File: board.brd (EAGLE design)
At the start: 80 x 80 mm, 47 parts, among them U1 MAX232

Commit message: added gitignore, tweaked board
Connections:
- removed net N$2: U1.12
- removed net N$20: U1.9
- removed net N$21: U1.10
- removed net N$9: U1.11
- net PC2: now also U1.12
- net PC3: now also U1.11
- net PC6: now also U1.9
- net PC7: now also U1.10
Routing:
- net PC2: track 25.1 -> 40.2 mm
- net PC7: track 12.8 -> 26.1 mm
- net PC3: track 23.2 -> 35.6 mm
- net PC6: track 16.4 -> 26.3 mm
- net GND: vias 21 -> 24
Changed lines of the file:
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@@
 <via x="69" y="63" extent="1-16" drill="0.305" shape="octagon"/>
 <contactref element="C3" pad="-"/>
+<via x="23" y="77" extent="1-16" drill="0.305" shape="octagon"/>
+<via x="24" y="73" extent="1-16" drill="0.305" shape="octagon"/>
+<via x="22" y="71" extent="1-16" drill="0.305" shape="octagon"/>
 <wire x1="44.784" y1="69.094" x2="44.784" y2="65.118" width="0" layer="19" extent="1-1"/>
 </signal>
@@
 <wire x1="33.608" y1="73.754" x2="29.417" y2="77.945" width="0.254" layer="1"/>
 <wire x1="29.417" y1="77.945" x2="27.385" y2="77.945" width="0.254" layer="1"/>
+<contactref element="U1" pad="12"/>
+<wire x1="15.635" y1="72.6" x2="15.635" y2="74.635" width="0.254" layer="1"/>
+<wire x1="15.635" y1="74.635" x2="18.945" y2="77.945" width="0.254" layer="1"/>
+<wire x1="18.945" y1="77.945" x2="27.385" y2="77.945" width="0.254" layer="1"/>
 </signal>
 <signal name="PC3">
@@
 <wire x1="32.592" y1="72.738" x2="32.592" y2="63.928478125" width="0.254" layer="1"/>
 <wire x1="32.592" y1="63.928478125" x2="38.281875" y2="58.238603125" width="0.254" layer="1"/>
+<contactref element="U1" pad="11"/>
+<wire x1="16.905" y1="72.6" x2="17" y2="72.695" width="0.4064" layer="1"/>
+<wire x1="17" y1="72.695" x2="17" y2="74" width="0.254" layer="1"/>
+<wire x1="17" y1="74" x2="18.405" y2="75.405" width="0.254" layer="1"/>
+<wire x1="18.405" y1="75.405" x2="27.385" y2="75.405" width="0.254" layer="1"/>
 </signal>
 <signal name="PC4">
@@
 <wire x1="29.798" y1="67.658" x2="29.798" y2="63.328365625" width="0.254" layer="1"/>
 <wire x1="29.798" y1="63.328365625" x2="36.58481875" y2="56.541546875" width="0.254" layer="1"/>
+<contactref element="U1" pad="9"/>
+<wire x1="27.385" y1="67.785" x2="22.57" y2="72.6" width="0.254" layer="1"/>
+<wire x1="22.57" y1="72.6" x2="19.445" y2="72.6" width="0.254" layer="1"/>
 </signal>
 <signal name="PC7">
@@
 <wire x1="36.019134375" y1="55.9758625" x2="27.385" y2="64.609996875" width="0.254" layer="1"/>
 <wire x1="27.385" y1="65.245" x2="27.385" y2="64.609996875" width="0.254" layer="1"/>
+<contactref element="U1" pad="10"/>
+<wire x1="22.63" y1="70" x2="27.385" y2="65.245" width="0.254" layer="1"/>
+<wire x1="18.175" y1="72.6" x2="18.175" y2="70.825" width="0.4064" layer="1"/>
+<wire x1="18.175" y1="70.825" x2="19" y2="70" width="0.254" layer="1"/>
+<wire x1="19" y1="70" x2="22.63" y2="70" width="0.254" layer="1"/>
 </signal>
 <signal name="PB0">
@@
 <wire x1="34.712" y1="41.904" x2="34.712" y2="40.226" width="0.254" layer="1"/>
 </signal>
-<signal name="N$2">
-<contactref element="U1" pad="12"/>
-</signal>
-<signal name="N$9">
-<contactref element="U1" pad="11"/>
-</signal>
-<signal name="N$20">
-<contactref element="U1" pad="9"/>
-</signal>
-<signal name="N$21">
-<contactref element="U1" pad="10"/>
-</signal>
 <signal name="AUX-TX">

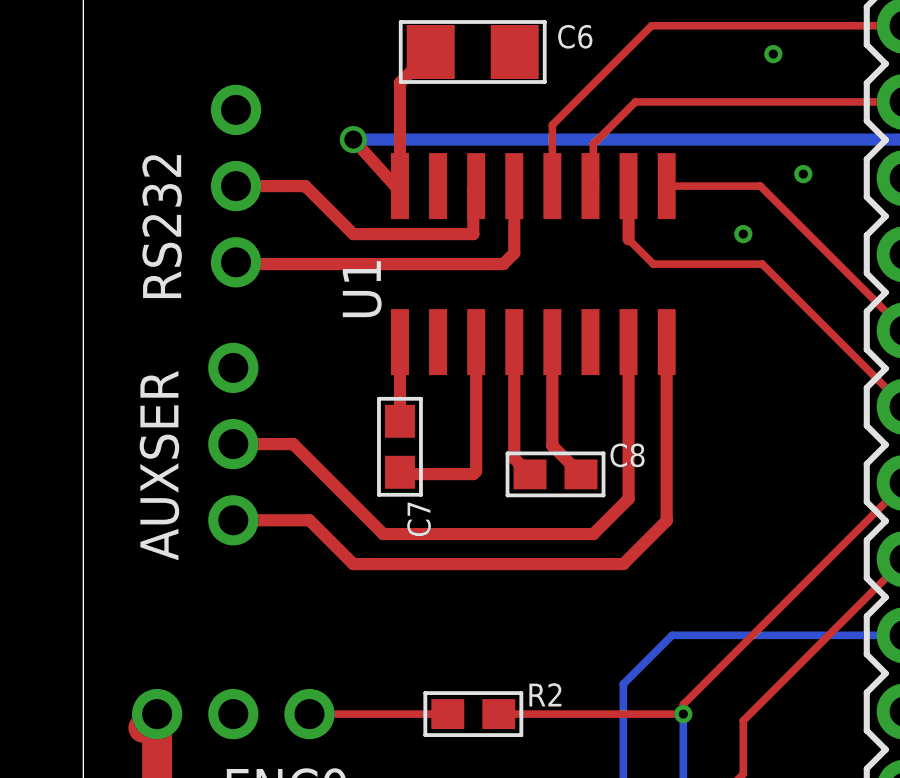
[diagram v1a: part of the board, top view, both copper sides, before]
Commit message: add some part values, nudge some traces
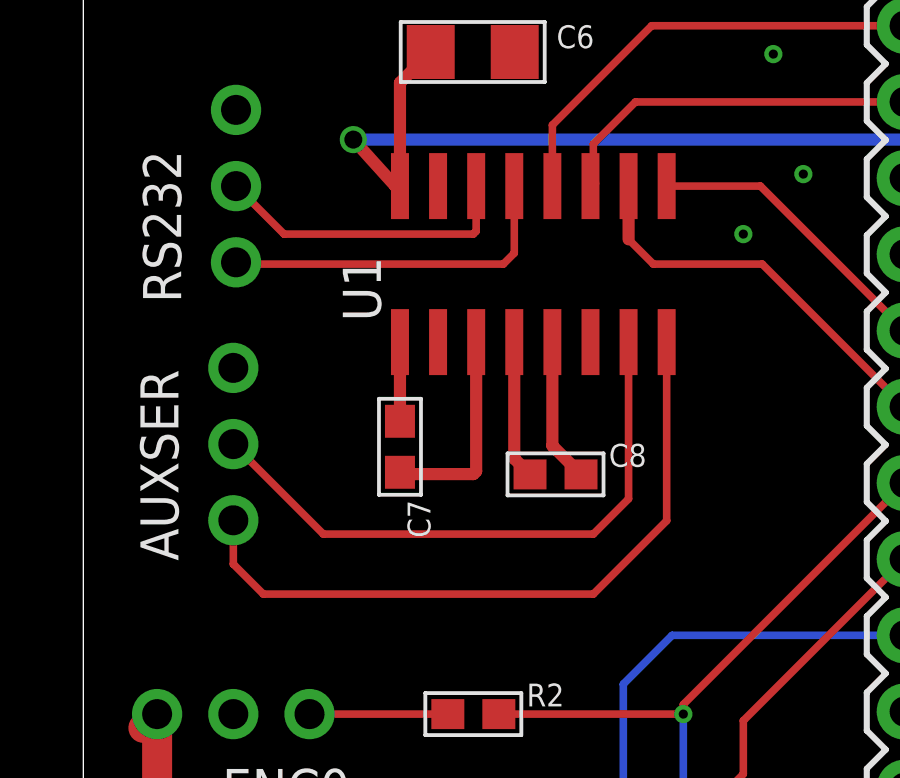
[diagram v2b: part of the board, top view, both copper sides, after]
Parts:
- C10, C9: value (none) -> 0.1uF
- C11: value (none) -> 18pF
- C12: value (none) -> 10pF
- C13, C14: value (none) -> 1uF
- C3: value (none) -> 470uF
- R1: value (none) -> 130O
- R2, R3, R4: value (none) -> 6.8k
- RN1: value (none) -> 10k
- RN2, RN3: value (none) -> 10K
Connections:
- net AUX-RX: now also AUXSER.2, U1.7; no longer AUXSER.1, U1.8
- net AUX-TX: now also AUXSER.1, U1.8; no longer AUXSER.2, U1.7
- net REMUS-RX: now also RS232.2, U1.14; no longer RS232.1, U1.13
- net REMUS-TX: now also RS232.1, U1.13; no longer RS232.2, U1.14
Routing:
- net AUX-TX: track 20.1 -> 23.3 mm
- net REMUS-RX: track 11.7 -> 10.2 mm
- net REMUS-TX: track 10.2 -> 11.7 mm
- net AUX-RX: track 21.6 -> 20.1 mm
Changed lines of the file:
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@@
 <element name="U$1" library="nonolith" package="SO-08" value="PCA9306" x="68.59" y="64.78" rot="R270"/>
 <element name="U1" library="nonolith" package="SO-16" value="MAX232" x="15" y="70"/>
-<element name="RN1" library="nonolith" package="RN8P-4R-CRA06S" value="" x="69.13" y="70.52" rot="R180"/>
+<element name="RN1" library="nonolith" package="RN8P-4R-CRA06S" value="10k" x="69.13" y="70.52" rot="R180"/>
 <element name="U$2" library="nonolith" package="NXT-FOOTPRINT" value="NXT-CONNECTOR" x="72.08" y="54.02" rot="R270"/>
 <element name="PT78" library="nonolith" package="1X03_ROUND" value="" x="11.09" y="16.49" rot="R90"/>
@@
 <element name="C1" library="microbuilder" package="EIA7343-31/D-W" value="470uF" x="62.1" y="75.82" rot="R180"/>
 <element name="C2" library="microbuilder" package="EIA7343-31/D-W" value="470uF" x="63.68" y="36.26"/>
-<element name="C3" library="microbuilder" package="EIA7343-31/D-W" value="" x="20.26" y="23.02" rot="R270"/>
+<element name="C3" library="microbuilder" package="EIA7343-31/D-W" value="470uF" x="20.26" y="23.02" rot="R270"/>
 <element name="C4" library="nonolith" package="1206" value="10uF" x="16.22" y="14.07"/>
 <element name="C5" library="nonolith" package="1206" value="10uF" x="65.4" y="40.93" rot="R180"/>
@@
 <element name="U$6" library="SparkFun" package="1X19" value="M19" x="52.785" y="32.225" smashed="yes" rot="R90"/>
 <element name="U$7" library="SparkFun" package="1X19" value="M19" x="27.385" y="32.225" smashed="yes" rot="R90"/>
-<element name="C9" library="nonolith" package="0603" value="" x="33.989" y="44.544" smashed="yes" rot="R180">
+<element name="C9" library="nonolith" package="0603" value="0.1uF" x="33.989" y="44.544" smashed="yes" rot="R180">
 <attribute name="NAME" x="32.846" y="45.687" size="0.762" layer="25" font="vector" ratio="12"/>
 <attribute name="VALUE" x="32.211" y="45.179" size="0.4064" layer="27" font="vector" rot="R180"/>
 </element>
-<element name="C10" library="nonolith" package="0603" value="" x="40.085" y="64.864" smashed="yes" rot="R180">
+<element name="C10" library="nonolith" package="0603" value="0.1uF" x="40.085" y="64.864" smashed="yes" rot="R180">
 <attribute name="NAME" x="41.609" y="63.594" size="0.762" layer="25" font="vector" ratio="12" rot="R180"/>
 </element>
@@
 <attribute name="VALUE" x="43.514" y="35.448" size="0.8128" layer="25" font="vector" ratio="10" rot="R180"/>
 </element>
-<element name="C11" library="nonolith" package="0603" value="" x="45.038" y="44.036" smashed="yes">
+<element name="C11" library="nonolith" package="0603" value="18pF" x="45.038" y="44.036" smashed="yes">
 <attribute name="NAME" x="43.514" y="42.004" size="0.762" layer="25" font="vector" ratio="12"/>
 </element>
-<element name="C12" library="nonolith" package="0603" value="" x="46.816" y="42.004" smashed="yes">
+<element name="C12" library="nonolith" package="0603" value="10pF" x="46.816" y="42.004" smashed="yes">
 <attribute name="NAME" x="47.07" y="43.274" size="0.762" layer="25" font="vector" ratio="12"/>
 </element>
 <element name="LED1" library="microbuilder" package="CHIPLED_0603" value="" x="33.608" y="42.258" rot="R270"/>
-<element name="R1" library="nonolith" package="0603" value="" x="33.862" y="40.226" smashed="yes" rot="R180">
+<element name="R1" library="nonolith" package="0603" value="130O" x="33.862" y="40.226" smashed="yes" rot="R180">
 <attribute name="NAME" x="35.386" y="38.956" size="0.762" layer="25" font="vector" ratio="10" rot="R180"/>
 </element>
-<element name="C13" library="nonolith" package="0603" value="" x="44.784" y="69.944" rot="R270"/>
-<element name="C14" library="nonolith" package="0603" value="" x="45.546" y="33.114"/>
-<element name="RN2" library="nonolith" package="RN8P-4R-CRA06S" value="" x="19" y="45" rot="R180"/>
-<element name="R2" library="nonolith" package="0603" value="" x="13" y="55"/>
-<element name="R3" library="nonolith" package="0603" value="" x="13" y="51"/>
-<element name="R4" library="nonolith" package="0603" value="" x="13" y="47"/>
+<element name="C13" library="nonolith" package="0603" value="1uF" x="44.784" y="69.944" rot="R270"/>
+<element name="C14" library="nonolith" package="0603" value="1uF" x="45.546" y="33.114"/>
+<element name="RN2" library="nonolith" package="RN8P-4R-CRA06S" value="10K" x="19" y="45" rot="R180"/>
+<element name="R2" library="nonolith" package="0603" value="6.8k" x="13" y="55"/>
+<element name="R3" library="nonolith" package="0603" value="6.8k" x="13" y="51"/>
+<element name="R4" library="nonolith" package="0603" value="6.8k" x="13" y="47"/>
 <element name="AUXSER" library="nonolith" package="1X03_ROUND" value="" x="5" y="64" rot="R90"/>
 <element name="MOT-THRUST" library="nonolith" package="1X03_ROUND" value="" x="13" y="30" rot="R270"/>
 <element name="3V3-I2C" library="nonolith" package="1X03_ROUND" value="" x="58" y="68" rot="R90"/>
 <element name="EXT_I2C" library="nonolith" package="1X04_ROUND" value="" x="64" y="51" rot="R270"/>
-<element name="RN3" library="nonolith" package="RN8P-4R-CRA06S" value="" x="17" y="38" rot="R270"/>
+<element name="RN3" library="nonolith" package="RN8P-4R-CRA06S" value="10K" x="17" y="38" rot="R270"/>
 </elements>
 <signals>
@@
 </signal>
 <signal name="REMUS-RX">
+<contactref element="U1" pad="14"/>
+<contactref element="RS232" pad="2"/>
+<wire x1="5.09" y1="72.6" x2="6.69" y2="71" width="0.254" layer="1"/>
+<wire x1="6.69" y1="71" x2="13" y2="71" width="0.254" layer="1"/>
+<wire x1="13" y1="71" x2="13.095" y2="71.095" width="0.254" layer="1"/>
+<wire x1="13.095" y1="71.095" x2="13.095" y2="72.6" width="0.254" layer="1"/>
+</signal>
+<signal name="REMUS-TX">
+<contactref element="U1" pad="13"/>
 <contactref element="RS232" pad="1"/>
-<contactref element="U1" pad="13"/>
-<wire x1="14.365" y1="72.6" x2="14.365" y2="70.365" width="0.4064" layer="1"/>
-<wire x1="14.365" y1="70.365" x2="14" y2="70" width="0.4064" layer="1"/>
-<wire x1="14" y1="70" x2="5.15" y2="70" width="0.4064" layer="1"/>
-<wire x1="5.15" y1="70" x2="5.09" y2="70.06" width="0.4064" layer="1"/>
-</signal>
-<signal name="REMUS-TX">
-<contactref element="RS232" pad="2"/>
-<contactref element="U1" pad="14"/>
-<wire x1="13.095" y1="72.6" x2="13" y2="72.505" width="0.4064" layer="1"/>
-<wire x1="13" y1="72.505" x2="13" y2="71" width="0.4064" layer="1"/>
-<wire x1="13" y1="71" x2="9" y2="71" width="0.4064" layer="1"/>
-<wire x1="9" y1="71" x2="7.4" y2="72.6" width="0.4064" layer="1"/>
-<wire x1="7.4" y1="72.6" x2="5.09" y2="72.6" width="0.4064" layer="1"/>
+<wire x1="5.09" y1="70.06" x2="5.15" y2="70" width="0.254" layer="1"/>
+<wire x1="5.15" y1="70" x2="14" y2="70" width="0.254" layer="1"/>
+<wire x1="14" y1="70" x2="14.365" y2="70.365" width="0.254" layer="1"/>
+<wire x1="14.365" y1="70.365" x2="14.365" y2="72.6" width="0.254" layer="1"/>
 </signal>
 <signal name="ENCO0">
@@
 </signal>
 <signal name="AUX-TX">
-<contactref element="AUXSER" pad="2"/>
-<contactref element="U1" pad="7"/>
-<wire x1="5" y1="64" x2="7" y2="64" width="0.4064" layer="1"/>
-<wire x1="7" y1="64" x2="10" y2="61" width="0.4064" layer="1"/>
-<wire x1="10" y1="61" x2="17" y2="61" width="0.4064" layer="1"/>
-<wire x1="17" y1="61" x2="18.175" y2="62.175" width="0.4064" layer="1"/>
-<wire x1="18.175" y1="67.4" x2="18.175" y2="62.175" width="0.4064" layer="1"/>
-</signal>
-<signal name="AUX-RX">
 <contactref element="U1" pad="8"/>
 <contactref element="AUXSER" pad="1"/>
-<wire x1="5" y1="61.46" x2="7.54" y2="61.46" width="0.4064" layer="1"/>
-<wire x1="7.54" y1="61.46" x2="9" y2="60" width="0.4064" layer="1"/>
-<wire x1="9" y1="60" x2="18" y2="60" width="0.4064" layer="1"/>
-<wire x1="18" y1="60" x2="19.445" y2="61.445" width="0.4064" layer="1"/>
-<wire x1="19.445" y1="67.4" x2="19.445" y2="61.445" width="0.4064" layer="1"/>
+<wire x1="5" y1="61.46" x2="5" y2="60" width="0.254" layer="1"/>
+<wire x1="5" y1="60" x2="6" y2="59" width="0.254" layer="1"/>
+<wire x1="6" y1="59" x2="17" y2="59" width="0.254" layer="1"/>
+<wire x1="17" y1="59" x2="19.445" y2="61.445" width="0.254" layer="1"/>
+<wire x1="19.445" y1="61.445" x2="19.445" y2="67.4" width="0.254" layer="1"/>
+</signal>
+<signal name="AUX-RX">
+<contactref element="U1" pad="7"/>
+<contactref element="AUXSER" pad="2"/>
+<wire x1="5" y1="64" x2="8" y2="61" width="0.254" layer="1"/>
+<wire x1="8" y1="61" x2="17" y2="61" width="0.254" layer="1"/>
+<wire x1="17" y1="61" x2="18.175" y2="62.175" width="0.254" layer="1"/>
+<wire x1="18.175" y1="62.175" x2="18.175" y2="67.4" width="0.254" layer="1"/>
 </signal>
 <signal name="PE3-P">
